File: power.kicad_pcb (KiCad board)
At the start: 2 copper layers, 99.9 x 99.7 mm, 210 parts, among them J1 USB_A, J2 Barrel_Jack_Switch, J3 Conn_02x06_Odd_Even, J4 Conn_02x10_Odd_Even, J5 Conn_02x06, J6 Conn_02x10_Odd_Even, J7 Conn_Coaxial, J8 Conn_Coaxial, Q1 MOSFET_P, T1 BALUN, T2 BALUN, U1 ZLDO1117G33TA, U10 lx9_XC6SLX9-TQ144, U11 FSM1LPTR, U12 FSM1LPTR, U13 FSM1LPTR, U14 SI5351C, U15 MAX5864, U16 MAX2830, U2 ZLDO1117G33TA, U3 ZLDO1117G33TA, U4 FSM1LPTR, U5 STM32F722ZET, U6 LSM9DS1, U7 Omega2+, U8 FSM1LPTR, U9 CY7C199, X1 Oscillator_ASE-xxxMHz, Y1 ABM8G-16.000MHZ-B4Y-T, Y2 Crystal, Y3 ABM8G-25.000MHZ-B4Y-T

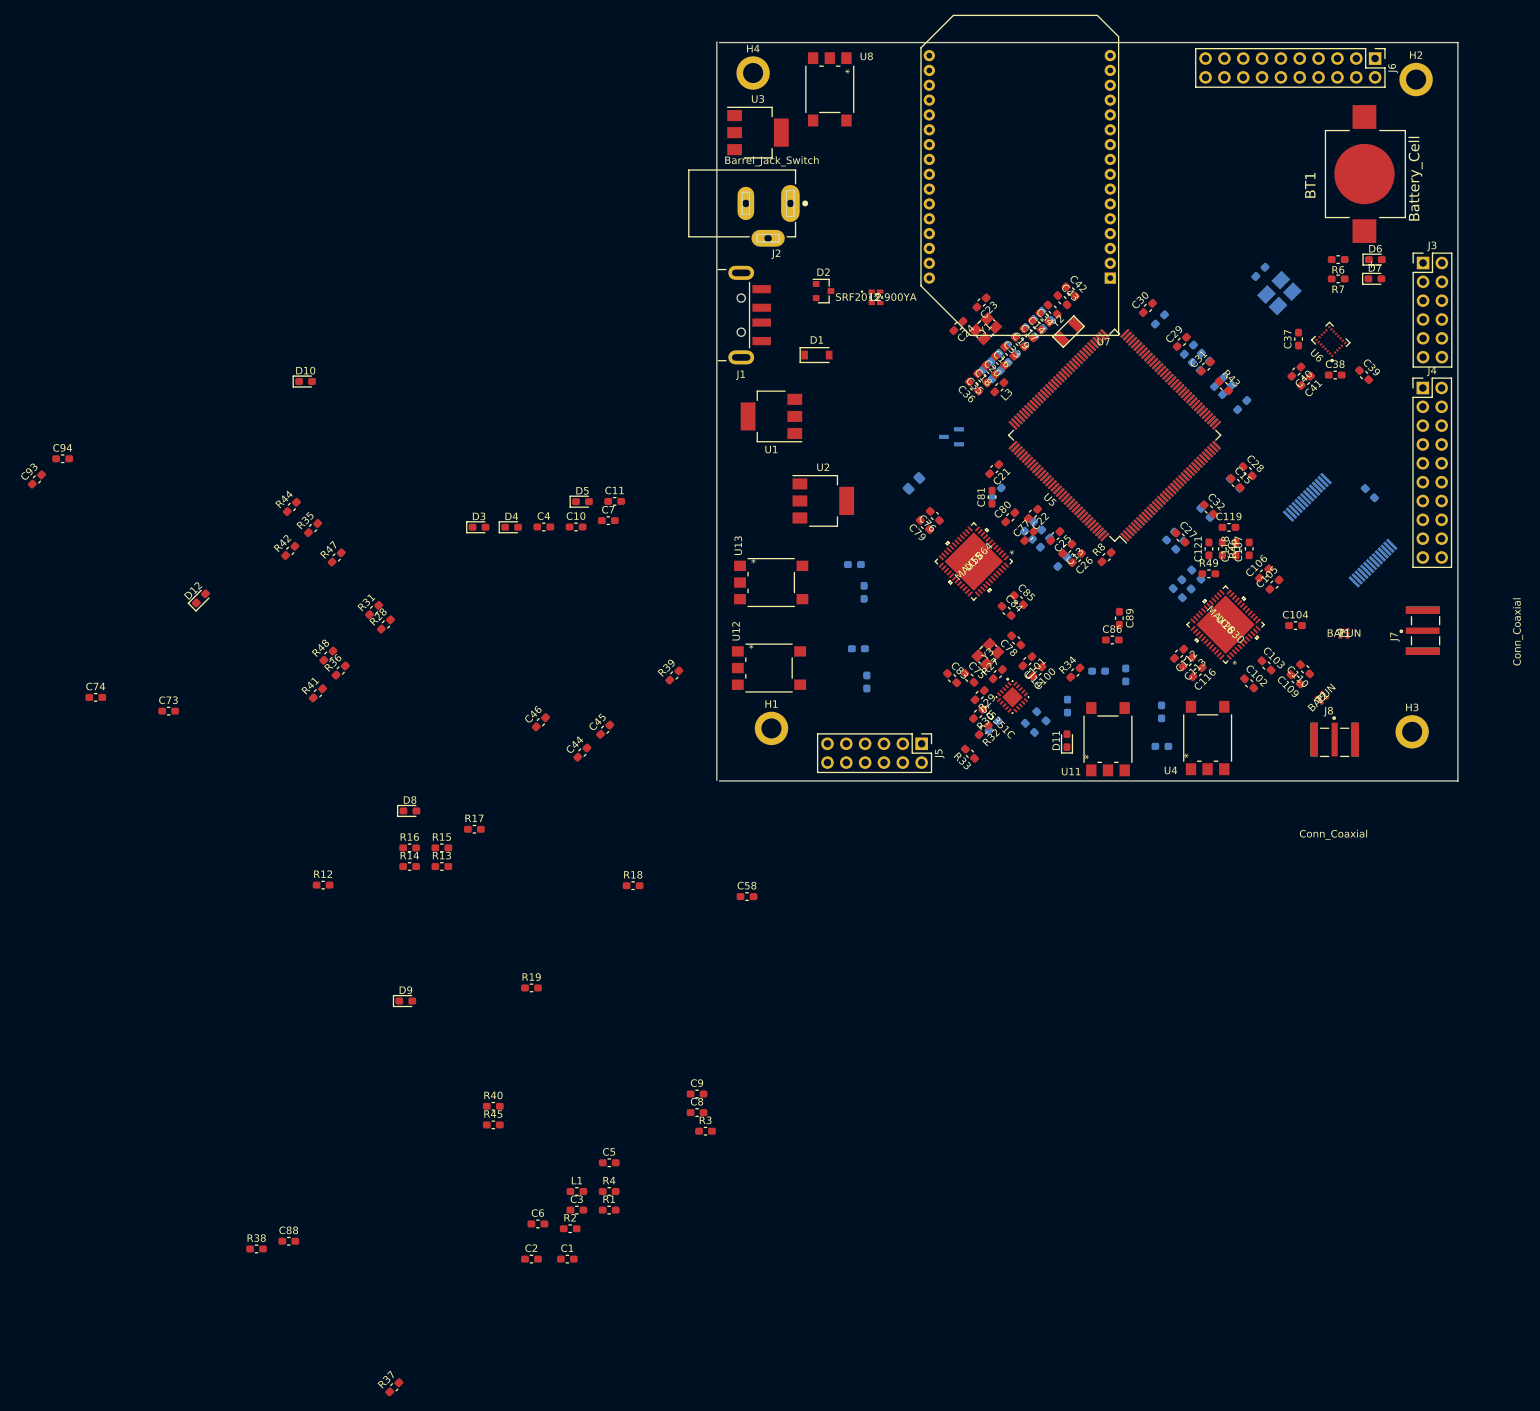
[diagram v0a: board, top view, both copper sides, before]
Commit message: diseño de esquematico fm
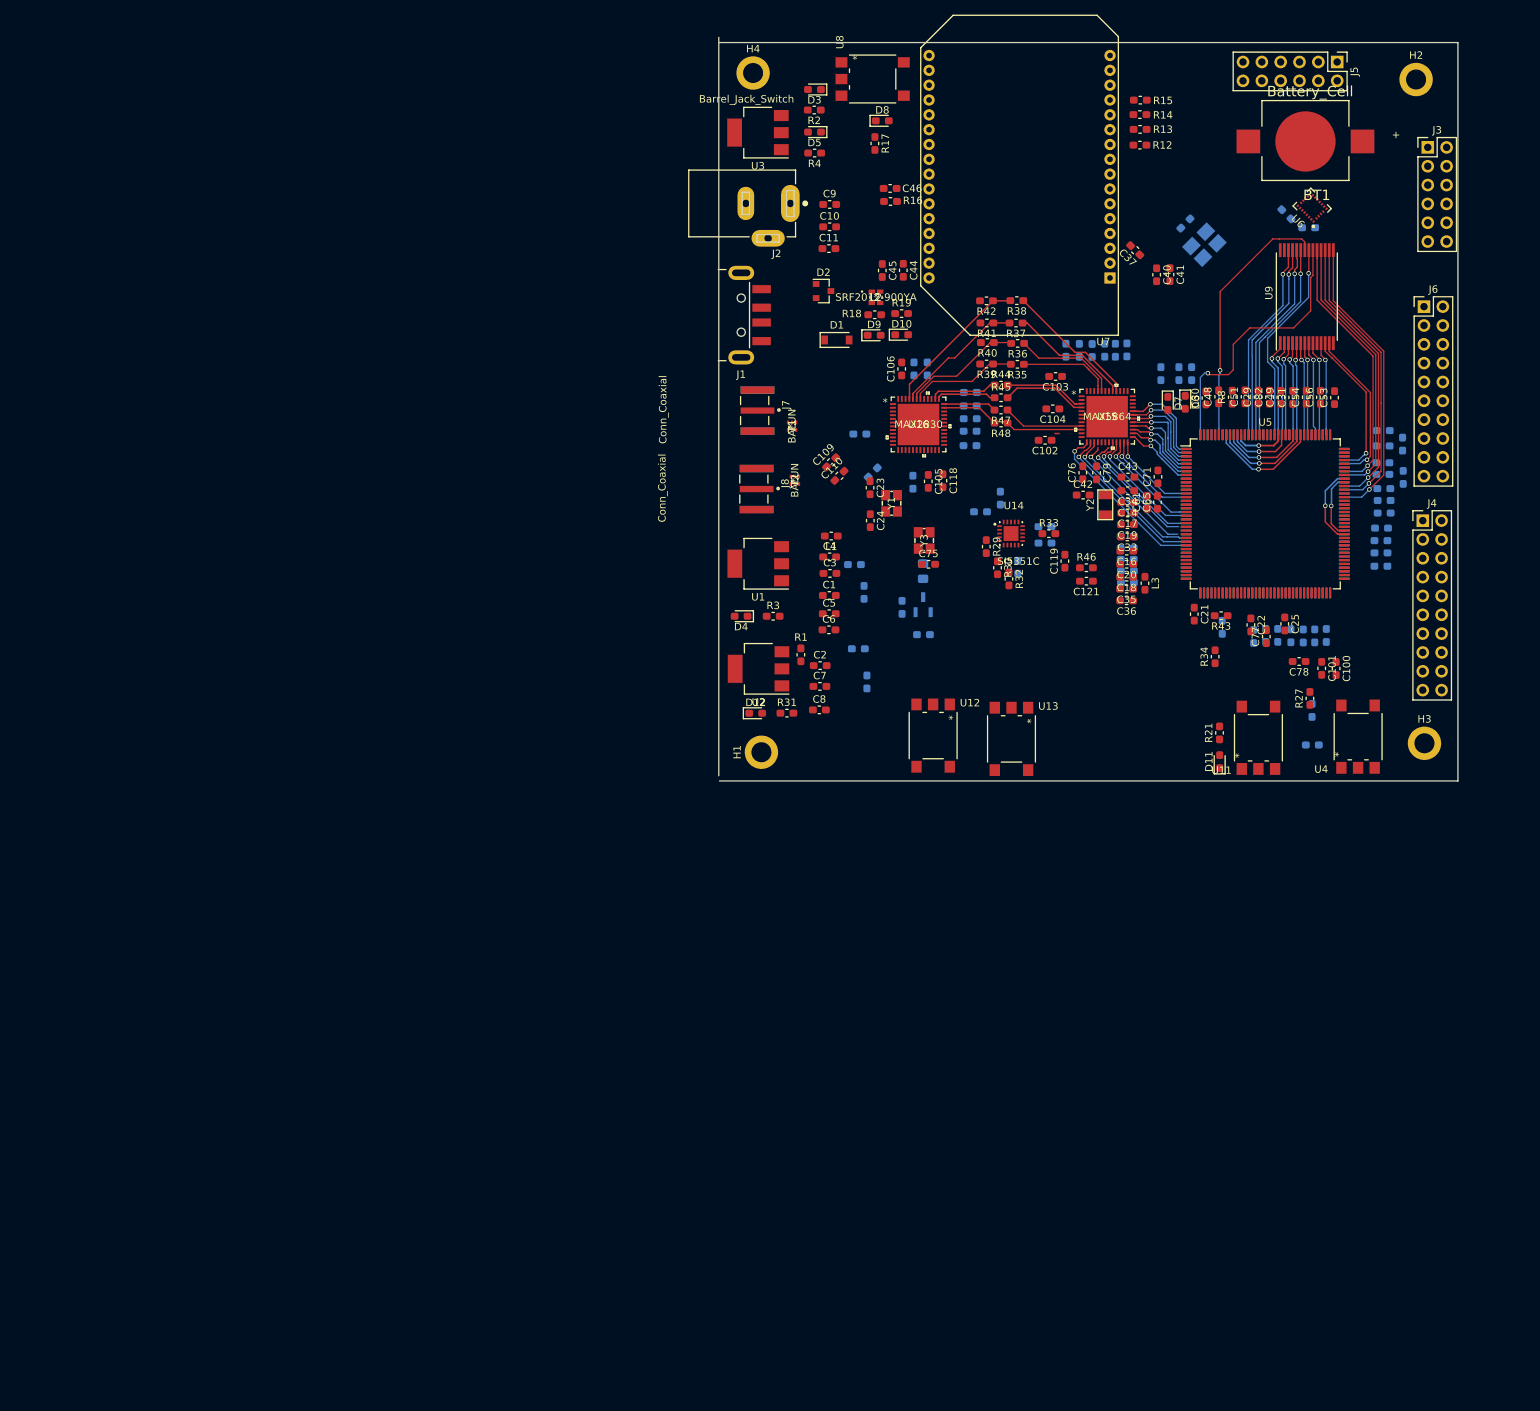
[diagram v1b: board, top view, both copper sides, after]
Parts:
- added R10: 1.5k, Resistor_SMD:R_0603_1608Metric_Pad1.05x0.95mm_HandSolder, B.Cu at (143.5, 73.9)
- added R9: 1.5k, Resistor_SMD:R_0603_1608Metric_Pad1.05x0.95mm_HandSolder, B.Cu at (143.4, 69.4)
- C107, C112, C113, C116, C13, C15, C26, C27, C28, C32, C38, C39, C58, C73, C74, C80, C81, C83, C84, C85, C86, C88, C89, C93, C94, R28, R49, R6, R7: moved to B.Cu
- C48, C49, C51, C53, C54, C56, C61, C65, C71, C82, R21, U9: moved to F.Cu
- moved R37 166.2 mm to (91.3, 53.1), turned to 180 degrees
- moved R38 163.9 mm to (91.4, 50.0), turned to 180 degrees
- moved C88 159.4 mm to (98.0, 56.7), turned to 90 degrees
- moved R2 154.4 mm to (64.1, 24.3), turned to 180 degrees
- moved R12 148.6 mm to (108.0, 29.1)
- moved C93 143.3 mm to (101.6, 56.8), turned to 90 degrees
- moved R4 142.7 mm to (64.1, 30.1), turned to 180 degrees
- moved R14 141.3 mm to (108.0, 25.0)
- moved R15 138.0 mm to (108.0, 23.0)
- moved C94 137.9 mm to (99.8, 56.7), turned to 90 degrees
- moved R13 136.9 mm to (108.0, 26.9)
- moved R40 122.7 mm to (87.4, 55.7), turned to 180 degrees
- moved C9 121.3 mm to (66.2, 37.1)
- moved R45 119.6 mm to (89.3, 63.1)
- moved D8 112.8 mm to (73.3, 25.8)
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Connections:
- C93 pad 1: (no net) -> /rf_front_end/COM
- C93 pad 2: (no net) -> GND
- C94 pad 1: (no net) -> /rf_front_end/REFN
- C94 pad 2: (no net) -> GND
- J6 pad 18: VCC_5V -> vcc_FPGA
- J6 pad 20: GND -> VCC_5V
- U10 pad 118: adDD0 -> adDA0
- U10 pad 119: adDD1 -> adDA1
- U10 pad 120: adDD2 -> adDA2
- U10 pad 121: adDD3 -> adDA3
- U10 pad 123: adDD4 -> adDA4
- U10 pad 124: adDD5 -> adDA5
- U10 pad 126: adDD6 -> adDA6
- U10 pad 127: adDD7 -> adDA7
- U10 pad 131: adDD8 -> adDD0
- U10 pad 132: adDD9 -> adDD1
- U10 pad 137: adDA0 -> adDD2
- U10 pad 138: adDA1 -> adDD3
- U10 pad 139: adDA2 -> adDD4
- U10 pad 14: /FPGA_spartan6/NEM_A0 -> /FPGA_spartan6/MEN_A4
- U10 pad 140: adDA3 -> adDD5
- U10 pad 141: adDA4 -> adDD6
- U10 pad 142: adDA5 -> adDD7
- U10 pad 143: adDA6 -> adDD8
- U10 pad 144: adDA7 -> adDD9
- U10 pad 15: /FPGA_spartan6/MEN_A1 -> /FPGA_spartan6/MEN_A3
- U10 pad 17: /FPGA_spartan6/MEN_A3 -> /FPGA_spartan6/MEN_A1
- U10 pad 21: /FPGA_spartan6/MEN_A4 -> /FPGA_spartan6/NEM_A0
- U10 pad 43: /FPGA_spartan6/MEN_D3 -> /FPGA_spartan6/MEN_D7
- U10 pad 44: /FPGA_spartan6/MEN_D4 -> /FPGA_spartan6/MEN_D6
- U10 pad 48: /FPGA_spartan6/MEN_D6 -> /FPGA_spartan6/MEN_D4
- U10 pad 50: /FPGA_spartan6/MEN_D7 -> /FPGA_spartan6/MEN_D3
- U10 pad 60: /FPGA_spartan6/FGPIO3 -> /FPGA_spartan6/FGPIO7
- U10 pad 66: /FPGA_spartan6/FGPIO7 -> /FPGA_spartan6/FGPIO3
- U10 pad 69: /FPGA_spartan6/FGPIO14 -> /FPGA_spartan6/FGPIO15
- U10 pad 70: Net-(U10-Pad70) -> /FPGA_spartan6/MEN_WE
- U10 pad 75: /FPGA_spartan6/FGPIO15 -> /FPGA_spartan6/FGPIO14
- U15 pad 40: /rf_front_end/QD+ -> /rf_front_end/ID+
- U15 pad 41: /rf_front_end/QD- -> /rf_front_end/ID-
- U15 pad 44: /rf_front_end/ID- -> /rf_front_end/QD-
- U15 pad 45: /rf_front_end/ID+ -> /rf_front_end/QD+
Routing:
- net /FPGA_spartan6/MEN_D3: track 0.00 -> 39.7 mm, vias 0 -> 1
- net /FPGA_spartan6/MEN_D4: track 0.00 -> 38.7 mm, vias 0 -> 1
- net /FPGA_spartan6/MEN_D5: track 0.00 -> 37.9 mm, vias 0 -> 1
- net /FPGA_spartan6/MEN_CE: track 0.00 -> 36.8 mm, vias 0 -> 1
- net /FPGA_spartan6/MEN_D6: track 0.00 -> 36.7 mm, vias 0 -> 1
- net /FPGA_spartan6/MEN_D7: track 0.00 -> 36.0 mm, vias 0 -> 1
- net /FPGA_spartan6/MEN_OE: track 0.00 -> 35.0 mm, vias 0 -> 1
- net (no net): track 0.00 -> 34.6 mm, vias 0 -> 2
- net /FPGA_spartan6/NEM_A0: track 0.00 -> 27.6 mm, vias 0 -> 1
- net /FPGA_spartan6/MEN_A2: track 0.00 -> 27.2 mm, vias 0 -> 1
- net /FPGA_spartan6/MEN_A1: track 0.00 -> 27.2 mm, vias 0 -> 1
- net /FPGA_spartan6/MEN_A3: track 0.00 -> 27.1 mm, vias 0 -> 1
- net /FPGA_spartan6/MEN_A4: track 0.00 -> 27.1 mm, vias 0 -> 1
- net adDA0: track 0.00 -> 23.3 mm, vias 0 -> 1
- net adDA1: track 0.00 -> 22.0 mm, vias 0 -> 1
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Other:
- board size 99.9 x 99.7 mm -> 99.7 x 100.3 mm
- net class ALI added: clearance 0.3, trace_width 6, via_dia 0.7, via_drill 0.5
- net class Default: via_dia 0.8 -> 0.6
- net class FREC added: clearance 0.2, trace_width 0.2, via_dia 0.5, via_drill 0.3
- rule trace_min: 0.2 -> 0.16

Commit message: diseño de esquematico CASI FINAL
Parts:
- C12, C27, C32, C38, C39, C52, C57, C58, C67, C70, C73, FB1, Q1, R25, R28, R49, R5: moved to F.Cu
- C16, C18, C19, C20, C21, C22, C25, C33, C35, C36, C40, C41, D2, L3, R43: moved to B.Cu
- moved U11 68.6 mm to (149.4, 50.5), turned to 0 degrees
- moved R18 68.0 mm to (103.2, 112.5), turned to 270 degrees
- moved D11 65.8 mm to (148.4, 53.4), turned to 180 degrees
- moved R19 65.5 mm to (100.5, 112.5), turned to 270 degrees
- moved D9 61.8 mm to (103.1, 108.2), turned to 90 degrees
- moved R21 60.6 mm to (144.5, 53.5), turned to 180 degrees
- moved D10 59.0 mm to (100.4, 108.3), turned to 90 degrees
- moved U4 58.5 mm to (148.7, 56.1), turned to 90 degrees
- moved C72 47.5 mm to (147.0, 74.0), turned to 315 degrees
- moved C78 46.7 mm to (88.2, 76.9)
- moved X1 44.0 mm to (144.1, 76.9), turned to 315 degrees
- moved R5 44.0 mm to (147.7, 69.2)
- moved C12 41.5 mm to (147.7, 67.2), turned to 0 degrees
- moved L1 39.6 mm to (63.1, 42.3), turned to 90 degrees
- moved C24 39.2 mm to (110.5, 84.6), turned to 90 degrees
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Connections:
- J3 pad 10: /STM32_micro/CS_A_G -> /STM32_micro/SDO_A_G
- J3 pad 3: /STM32_micro/INT_M -> /STM32_micro/INT1_A_G
- J3 pad 5: /STM32_micro/DRDY_M -> /STM32_micro/INT_M
- J3 pad 6: /STM32_micro/INT1_A_G -> /STM32_micro/DRDY_M
- J3 pad 7: /STM32_micro/SDO_M -> /STM32_micro/CS_M
- J3 pad 8: /STM32_micro/SDO_A_G -> /STM32_micro/CS_A_G
- J3 pad 9: /STM32_micro/CS_M -> /STM32_micro/SDO_M
- J4 pad 10: /STM32_micro/GPIO_11 -> /STM32_micro/GPIO_07
- J4 pad 11: /STM32_micro/GPIO_04 -> /STM32_micro/GPIO_08
- J4 pad 12: /STM32_micro/GPIO_12 -> /STM32_micro/GPIO_09
- J4 pad 13: /STM32_micro/GPIO_05 -> /STM32_micro/GPIO_10
- J4 pad 14: /STM32_micro/GPIO_13 -> /STM32_micro/GPIO_11
- J4 pad 15: /STM32_micro/GPIO_06 -> /STM32_micro/GPIO_12
- J4 pad 16: /STM32_micro/GPIO_14 -> /STM32_micro/GPIO_13
- J4 pad 17: /STM32_micro/GPIO_07 -> /STM32_micro/GPIO_14
- J4 pad 4: /STM32_micro/GPIO_08 -> /STM32_micro/GPIO_01
- J4 pad 5: /STM32_micro/GPIO_01 -> /STM32_micro/GPIO_02
- J4 pad 6: /STM32_micro/GPIO_09 -> /STM32_micro/GPIO_03
- J4 pad 7: /STM32_micro/GPIO_02 -> /STM32_micro/GPIO_04
- J4 pad 8: /STM32_micro/GPIO_10 -> /STM32_micro/GPIO_05
- J4 pad 9: /STM32_micro/GPIO_03 -> /STM32_micro/GPIO_06
- J5 pad 10: /ONION_OMEGA/MOSI -> /ONION_OMEGA/SPI_CS
- J5 pad 11: /ONION_OMEGA/MISO -> VCC_5V
- J5 pad 2: I2C_SCL -> GND
- J5 pad 4: /ONION_OMEGA/RX_PIN -> /ONION_OMEGA/MISO
- J5 pad 5: /ONION_OMEGA/TX_PIN -> I2C_SCL
- J5 pad 6: VCC_5V -> /ONION_OMEGA/MOSI
- J5 pad 7: GND -> /ONION_OMEGA/RX_PIN
- J5 pad 8: /ONION_OMEGA/SPI_CS -> /ONION_OMEGA/SPI_CLK
- J5 pad 9: /ONION_OMEGA/SPI_CLK -> /ONION_OMEGA/TX_PIN
- U10 pad 104: /FPGA_spartan6/FGPIO11 -> /FPGA_spartan6/FGPIO14
- U10 pad 105: /FPGA_spartan6/FGPIO9 -> /FPGA_spartan6/FGPIO6
- U10 pad 39: /FPGA_spartan6/FGPIO10 -> /FPGA_spartan6/FGPIO9
- U10 pad 56: /FPGA_spartan6/FGPIO2 -> /FPGA_spartan6/FGPIO1
- U10 pad 57: /FPGA_spartan6/FGPIO4 -> /FPGA_spartan6/FGPIO10
- U10 pad 58: /FPGA_spartan6/FGPIO6 -> /FPGA_spartan6/FGPIO2
- U10 pad 59: /FPGA_spartan6/FGPIO1 -> /FPGA_spartan6/FGPIO11
- U10 pad 65: /FPGA_spartan6/FGPIO5 -> /FPGA_spartan6/FGPIO3
- U10 pad 66: /FPGA_spartan6/FGPIO3 -> /FPGA_spartan6/FGPIO12
- U10 pad 67: /FPGA_spartan6/FGPIO12 -> /FPGA_spartan6/FGPIO4
- U10 pad 75: /FPGA_spartan6/FGPIO14 -> /FPGA_spartan6/FGPIO13
- U10 pad 80: /FPGA_spartan6/FGPIO13 -> /FPGA_spartan6/FGPIO5
- U5 pad 18: /STM32_micro/GPIO_10 -> /STM32_micro/GPIO_15
- U5 pad 19: /STM32_micro/GPIO_11 -> /STM32_micro/GPIO_14
- U5 pad 2: Net-(U5-Pad2) -> /STM32_micro/LED1
- U5 pad 20: /STM32_micro/GPIO_12 -> /STM32_micro/GPIO_13
- U5 pad 21: /STM32_micro/GPIO_13 -> /STM32_micro/GPIO_12
- U5 pad 22: /STM32_micro/GPIO_14 -> /STM32_micro/GPIO_11
- U5 pad 26: /STM32_micro/GPIO_06 -> /STM32_micro/GPIO_10
- U5 pad 27: /STM32_micro/GPIO_07 -> /STM32_micro/GPIO_09
- U5 pad 29: /STM32_micro/GPIO_09 -> /STM32_micro/GPIO_07
- U5 pad 3: Net-(U5-Pad3) -> /STM32_micro/LED2
- U5 pad 35: SPI1_RSSI -> rf_RXHP
- U5 pad 36: rf_RXHP -> SPI1_RSSI
- U5 pad 4: /STM32_micro/LED1 -> Net-(U5-Pad4)
- U5 pad 49: /STM32_micro/GPIO_15 -> /STM32_micro/GPIO_06
- U5 pad 5: /STM32_micro/LED2 -> Net-(U5-Pad5)
- U5 pad 69: /STM32_micro/GPIO_00 -> /STM32_micro/GPIO_04
- U5 pad 70: /STM32_micro/GPIO_01 -> /STM32_micro/GPIO_05
- U5 pad 75: /STM32_micro/GPIO_04 -> /STM32_micro/GPIO_00
- U5 pad 76: /STM32_micro/GPIO_05 -> /STM32_micro/GPIO_01
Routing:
- net I2C_SDA: track 0.00 -> 214.3 mm, vias 0 -> 6
- net I2C_SCL: track 0.00 -> 194.8 mm, vias 0 -> 4
- net JNRST: track 0.00 -> 122.6 mm, vias 0 -> 5
- net SPI1_SCK: track 0.00 -> 110.2 mm, vias 0 -> 2
- net /FPGA_spartan6/FSW_1: track 0.00 -> 100.3 mm, vias 0 -> 6
- net SPI1_MISO: track 0.00 -> 94.7 mm, vias 0 -> 5
- net rf_ANTSEL: track 0.00 -> 91.9 mm, vias 0 -> 2
- net VCC_5V: track 0.00 -> 84.0 mm, vias 0 -> 2
- net rf_RXTX: track 0.00 -> 82.6 mm, vias 0 -> 2
- net /FPGA_spartan6/FSW_2: track 0.00 -> 82.0 mm, vias 0 -> 9
- net rf_RXHP: track 0.00 -> 78.6 mm, vias 0 -> 2
- net JTMS: track 0.00 -> 76.9 mm, vias 0 -> 4
- net JTCK: track 0.00 -> 76.3 mm, vias 0 -> 4
- net USART_TX: track 0.00 -> 75.2 mm, vias 0 -> 1
- net USART_RX: track 0.00 -> 75.2 mm, vias 0 -> 1
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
